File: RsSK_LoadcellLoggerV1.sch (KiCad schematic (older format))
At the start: 23 parts, among them P1 STLINK_SWD, U1 STM32F303RE, U2 TWE-Lite_DIP

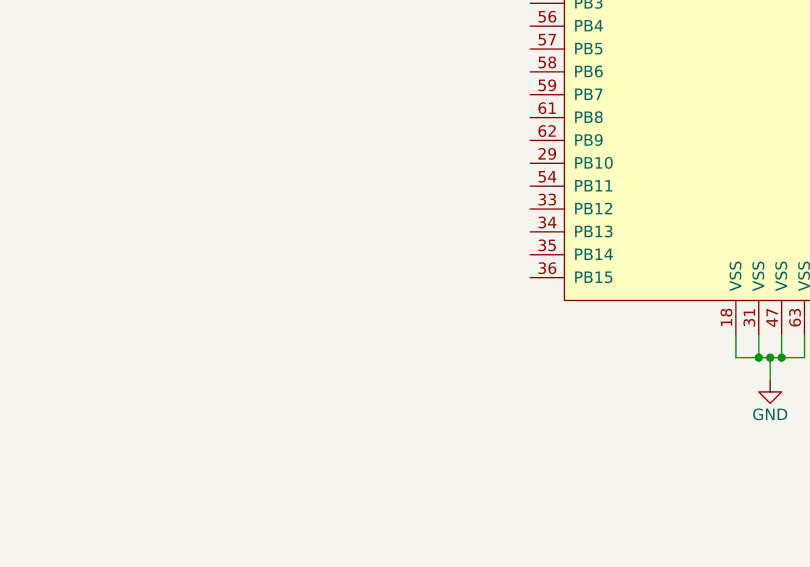
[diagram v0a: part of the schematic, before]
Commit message: add 4 led status indicators
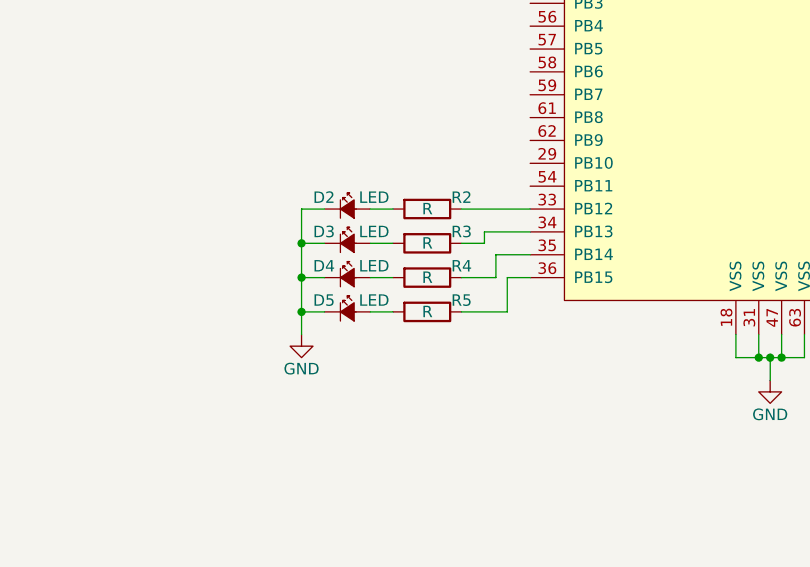
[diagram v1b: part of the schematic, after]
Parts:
- added D2, D3, D4, D5: LED, symbol LED_Small_ALT
- added R2, R3, R4, R5: R, symbol R
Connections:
- wire segments 60 -> 79
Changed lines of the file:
@@
 NoConn ~ 6750 6650
 NoConn ~ 6500 6650
+$Comp
+L LED_Small_ALT D2
+U 1 1 5A7AB50B
+P 3950 4800
+F 0 "D2" H 3800 4850 50  0000 L CNN
+F 1 "LED" H 4000 4850 50  0000 L CNN
+F 2 "" V 3950 4800 50  0001 C CNN
+F 3 "" V 3950 4800 50  0001 C CNN
+	1    3950 4800
+	1    0    0    -1
+$EndComp
+$Comp
+L R R2
+U 1 1 5A7AB9C5
+P 4300 4800
+F 0 "R2" V 4250 4950 50  0000 C CNN
+F 1 "R" V 4300 4800 50  0000 C CNN
+F 2 "" V 4230 4800 50  0001 C CNN
+F 3 "" H 4300 4800 50  0001 C CNN
+	1    4300 4800
+	0    1    1    0
+$EndComp
+Wire Wire Line
+	4150 4800 4050 4800
+$Comp
+L LED_Small_ALT D3
+U 1 1 5A7ABBC2
+P 3950 4950
+F 0 "D3" H 3800 5000 50  0000 L CNN
+F 1 "LED" H 4000 5000 50  0000 L CNN
+F 2 "" V 3950 4950 50  0001 C CNN
+F 3 "" V 3950 4950 50  0001 C CNN
+	1    3950 4950
+	1    0    0    -1
+$EndComp
+$Comp
+L R R3
+U 1 1 5A7ABBC8
+P 4300 4950
+F 0 "R3" V 4250 5100 50  0000 C CNN
+F 1 "R" V 4300 4950 50  0000 C CNN
+F 2 "" V 4230 4950 50  0001 C CNN
+F 3 "" H 4300 4950 50  0001 C CNN
+	1    4300 4950
+	0    1    1    0
+$EndComp
+Wire Wire Line
+	4150 4950 4050 4950
+$Comp
+L LED_Small_ALT D4
+U 1 1 5A7ABEC1
+P 3950 5100
+F 0 "D4" H 3800 5150 50  0000 L CNN
+F 1 "LED" H 4000 5150 50  0000 L CNN
+F 2 "" V 3950 5100 50  0001 C CNN
+F 3 "" V 3950 5100 50  0001 C CNN
+	1    3950 5100
+	1    0    0    -1
+$EndComp
+$Comp
+L R R4
+U 1 1 5A7ABEC7
+P 4300 5100
+F 0 "R4" V 4250 5250 50  0000 C CNN
+F 1 "R" V 4300 5100 50  0000 C CNN
+F 2 "" V 4230 5100 50  0001 C CNN
+F 3 "" H 4300 5100 50  0001 C CNN
+	1    4300 5100
+	0    1    1    0
+$EndComp
+Wire Wire Line
+	4150 5100 4050 5100
+$Comp
+L LED_Small_ALT D5
+U 1 1 5A7ABECE
+P 3950 5250
+F 0 "D5" H 3800 5300 50  0000 L CNN
+F 1 "LED" H 4000 5300 50  0000 L CNN
+F 2 "" V 3950 5250 50  0001 C CNN
+F 3 "" V 3950 5250 50  0001 C CNN
+	1    3950 5250
+	1    0    0    -1
+$EndComp
+$Comp
+L R R5
+U 1 1 5A7ABED4
+P 4300 5250
+F 0 "R5" V 4250 5400 50  0000 C CNN
+F 1 "R" V 4300 5250 50  0000 C CNN
+F 2 "" V 4230 5250 50  0001 C CNN
+F 3 "" H 4300 5250 50  0001 C CNN
+	1    4300 5250
+	0    1    1    0
+$EndComp
+Wire Wire Line
+	4150 5250 4050 5250
+Wire Wire Line
+	4650 5250 4650 5100
+Wire Wire Line
+	4650 5100 4750 5100
+Wire Wire Line
+	4750 5000 4600 5000
+Wire Wire Line
+	4600 5000 4600 5100
+Wire Wire Line
+	4750 4900 4550 4900
+Wire Wire Line
+	4550 4900 4550 4950
+Wire Wire Line
+	4550 4950 4450 4950
+Wire Wire Line
+	4600 5100 4450 5100
+Wire Wire Line
+	4650 5250 4450 5250
+Wire Wire Line
+	4450 4800 4750 4800
+$Comp
+L GND #PWR?
+U 1 1 5A7AC525
+P 3750 5350
+F 0 "#PWR?" H 3750 5100 50  0001 C CNN
+F 1 "GND" H 3750 5200 50  0000 C CNN
+F 2 "" H 3750 5350 50  0001 C CNN
+F 3 "" H 3750 5350 50  0001 C CNN
+	1    3750 5350
+	1    0    0    -1
+$EndComp
+Wire Wire Line
+	3750 4800 3750 5350
+Wire Wire Line
+	3750 5250 3850 5250
+Wire Wire Line
+	3750 5100 3850 5100
+Connection ~ 3750 5250
+Wire Wire Line
+	3850 4950 3750 4950
+Connection ~ 3750 5100
+Wire Wire Line
+	3850 4800 3750 4800
+Connection ~ 3750 4950
 $EndSCHEMATC
